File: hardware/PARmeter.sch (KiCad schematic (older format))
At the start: 45 parts, among them J1 USB_B_Micro, J2 Micro_SD_Card_Det_Hirose_DM3AT, J3 Conn_01x02, J4 Conn_01x09, SW1 KMR2, SW2 HRO_K1-520XUA-XX, U1 AP2112K-3.3, U2 STM32F103C8Tx, U3 MCP6002-xSN, U4 IP4234CZ6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

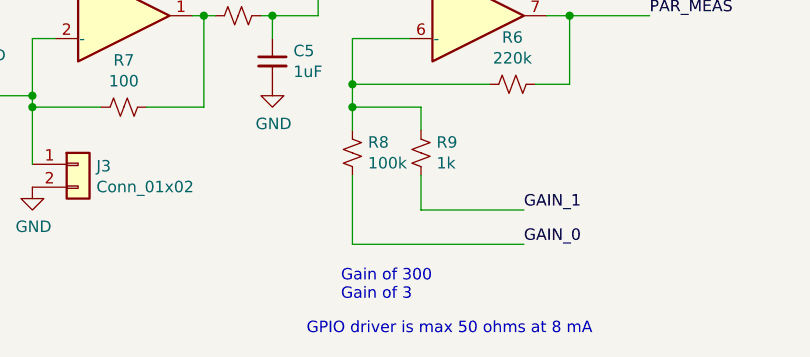
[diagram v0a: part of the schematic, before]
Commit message: fixed gain values + explicitly set gain outputs
- Math is hard
- Shouldn’t be necessary, but doesn’t hurt.
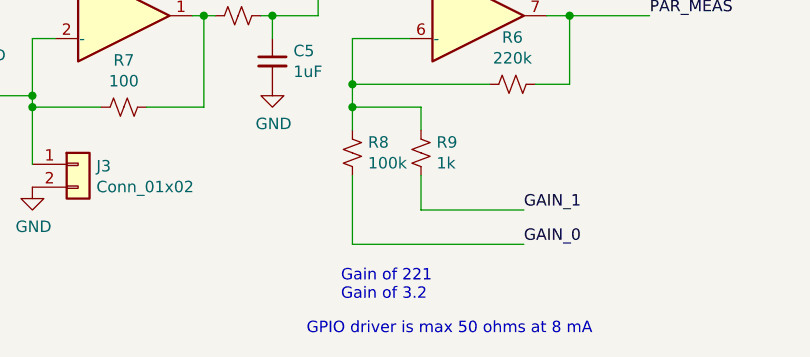
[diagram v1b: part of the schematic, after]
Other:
- note added: "Gain of 221\nGain of 3.2"
- note removed: "Gain of 300\nGain of 3"
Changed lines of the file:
@@
 Approx. 3mA full sunlight\nApprox. 0.3uA dim room\nDesign for 0.1 uA to 10 mA
 Text Notes 3650 7200 0    50   ~ 0
-Gain of 300\nGain of 3
+Gain of 221\nGain of 3.2
 $Comp
 L Device:C_Small C11

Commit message: Ditched dual-gain mode
There is a problem where the GPIO LOW state pulls to ~3.5mV rather than
0V as expected due to [supply current] * [resistance between the IC
ground and PCB ground]. Using superposition, this ~3.5 mV sees an
inverting amplifier with gain -Rf/Rs and causes an offset in the
measured value, unfortunately limiting our low-end sensitivity. I
mitigated this by increasing the transimpedance gain and reducing the
voltage gain. With some averaging, we get clean measurements in the
range of interest.
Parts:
- C5: value 1uF -> 4.7uF
- R5: value 100k -> 10k
- R6: value 220k -> 0
- R7: value 100 -> 1k
- R8: value 100k -> NO_STUFF
- R9: value 1k -> NO_STUFF
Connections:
- no-connect marks 4 -> 14
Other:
- note removed: "Approx. 3mA full sunlight\nApprox. 0.3uA dim room\nDesign for 0.1 uA to 10 mA"
- note removed: "Gain of 221\nGain of 3.2"
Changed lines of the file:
@@
 P 3700 6550
 F 0 "R8" H 3768 6596 50  0000 L CNN
-F 1 "100k" H 3768 6505 50  0000 L CNN
+F 1 "NO_STUFF" H 3768 6505 50  0000 L CNN
 F 2 "Resistor_SMD:R_0805_2012Metric" H 3700 6550 50  0001 C CNN
 F 3 "~" H 3700 6550 50  0001 C CNN
 	1    3700 6550
-	1    0    0    -1
+	-1   0    0    -1
 $EndComp
 $Comp
@@
 P 4000 6550
 F 0 "R9" H 4068 6596 50  0000 L CNN
-F 1 "1k" H 4068 6505 50  0000 L CNN
+F 1 "NO_STUFF" H 4068 6505 50  0000 L CNN
 F 2 "Resistor_SMD:R_0805_2012Metric" H 4000 6550 50  0001 C CNN
 F 3 "~" H 4000 6550 50  0001 C CNN
@@
 P 4400 6250
 F 0 "R6" V 4195 6250 50  0000 C CNN
-F 1 "220k" V 4286 6250 50  0000 C CNN
+F 1 "0" V 4286 6250 50  0000 C CNN
 F 2 "Resistor_SMD:R_0805_2012Metric" H 4400 6250 50  0001 C CNN
 F 3 "~" H 4400 6250 50  0001 C CNN
@@
 P 3200 5950
 F 0 "R5" V 2995 5950 50  0000 C CNN
-F 1 "100k" V 3086 5950 50  0000 C CNN
+F 1 "10k" V 3086 5950 50  0000 C CNN
 F 2 "Resistor_SMD:R_0805_2012Metric" H 3200 5950 50  0001 C CNN
 F 3 "~" H 3200 5950 50  0001 C CNN
@@
 P 2700 6350
 F 0 "R7" V 2495 6350 50  0000 C CNN
-F 1 "100" V 2586 6350 50  0000 C CNN
+F 1 "1k" V 2586 6350 50  0000 C CNN
 F 2 "Resistor_SMD:R_0805_2012Metric" H 2700 6350 50  0001 C CNN
 F 3 "~" H 2700 6350 50  0001 C CNN
@@
 Text Label 5000 5950 0    50   ~ 0
 PAR_MEAS
-Text Notes 800  5550 0    50   ~ 0
-Approx. 3mA full sunlight\nApprox. 0.3uA dim room\nDesign for 0.1 uA to 10 mA
-Text Notes 3650 7200 0    50   ~ 0
-Gain of 221\nGain of 3.2
 $Comp
 L Device:C_Small C11
@@
 P 3350 6150
 F 0 "C5" H 3442 6196 50  0000 L CNN
-F 1 "1uF" H 3442 6105 50  0000 L CNN
+F 1 "4.7uF" H 3442 6105 50  0000 L CNN
 F 2 "Capacitor_SMD:C_0805_2012Metric" H 3350 6150 50  0001 C CNN
 F 3 "~" H 3350 6150 50  0001 C CNN
@@
 Wire Wire Line
 	7550 4300 7850 4300
+NoConn ~ 7500 5600
+NoConn ~ 6200 5200
+NoConn ~ 6200 5100
+NoConn ~ 6200 4800
+NoConn ~ 6200 4700
+NoConn ~ 6200 4550
+NoConn ~ 6200 4500
+NoConn ~ 6200 4400
+NoConn ~ 6200 4200
+NoConn ~ 6200 4100
 $EndSCHEMATC

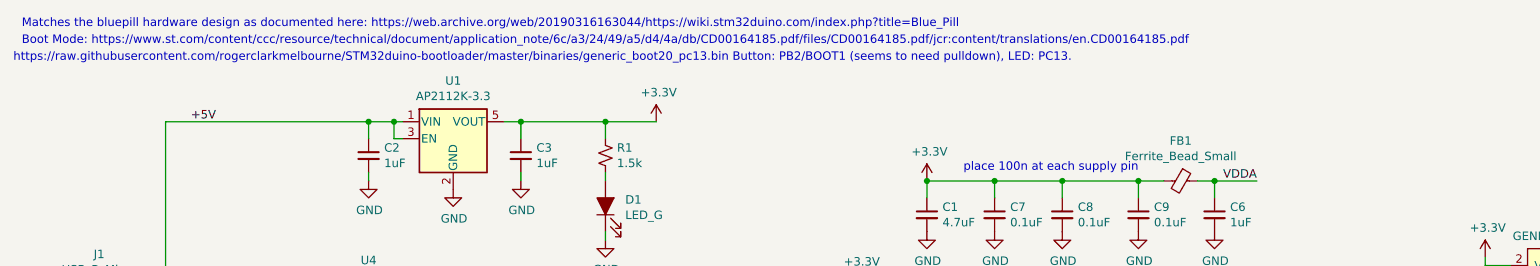
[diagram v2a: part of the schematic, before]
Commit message: Tested micro SD card, confirmed working
See title
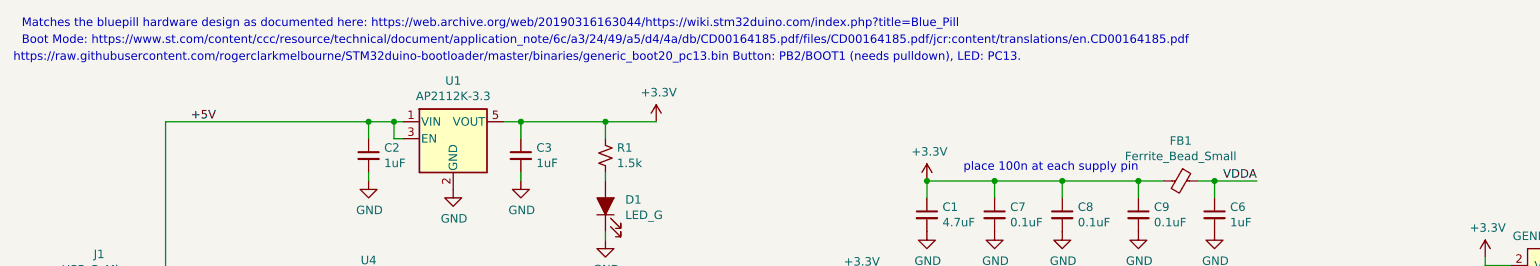
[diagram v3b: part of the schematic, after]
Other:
- note added: "https://raw.githubusercontent.com/rogerclarkmelbourne/STM32duino-bootloader/master/binaries/generic_boot20_pc13.bin Button: PB2/BOOT1 (needs pulldown), LED: PC13."
- note removed: "https://raw.githubusercontent.com/rogerclarkmelbourne/STM32duino-bootloader/master/binaries/generic_boot20_pc13.bin Button: PB2/BOOT1 (seems to need pulldown), LED: PC13."
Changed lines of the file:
@@
 $EndComp
 Text Notes 550  850  0    50   ~ 0
-https://raw.githubusercontent.com/rogerclarkmelbourne/STM32duino-bootloader/master/binaries/generic_boot20_pc13.bin Button: PB2/BOOT1 (seems to need pulldown), LED: PC13.
+https://raw.githubusercontent.com/rogerclarkmelbourne/STM32duino-bootloader/master/binaries/generic_boot20_pc13.bin Button: PB2/BOOT1 (needs pulldown), LED: PC13.
 $Comp
 L Device:R_Small_US R13
